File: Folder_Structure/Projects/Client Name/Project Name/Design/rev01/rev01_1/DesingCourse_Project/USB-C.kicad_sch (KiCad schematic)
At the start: 1 part, among them J7 TYPE-C-31-M-12

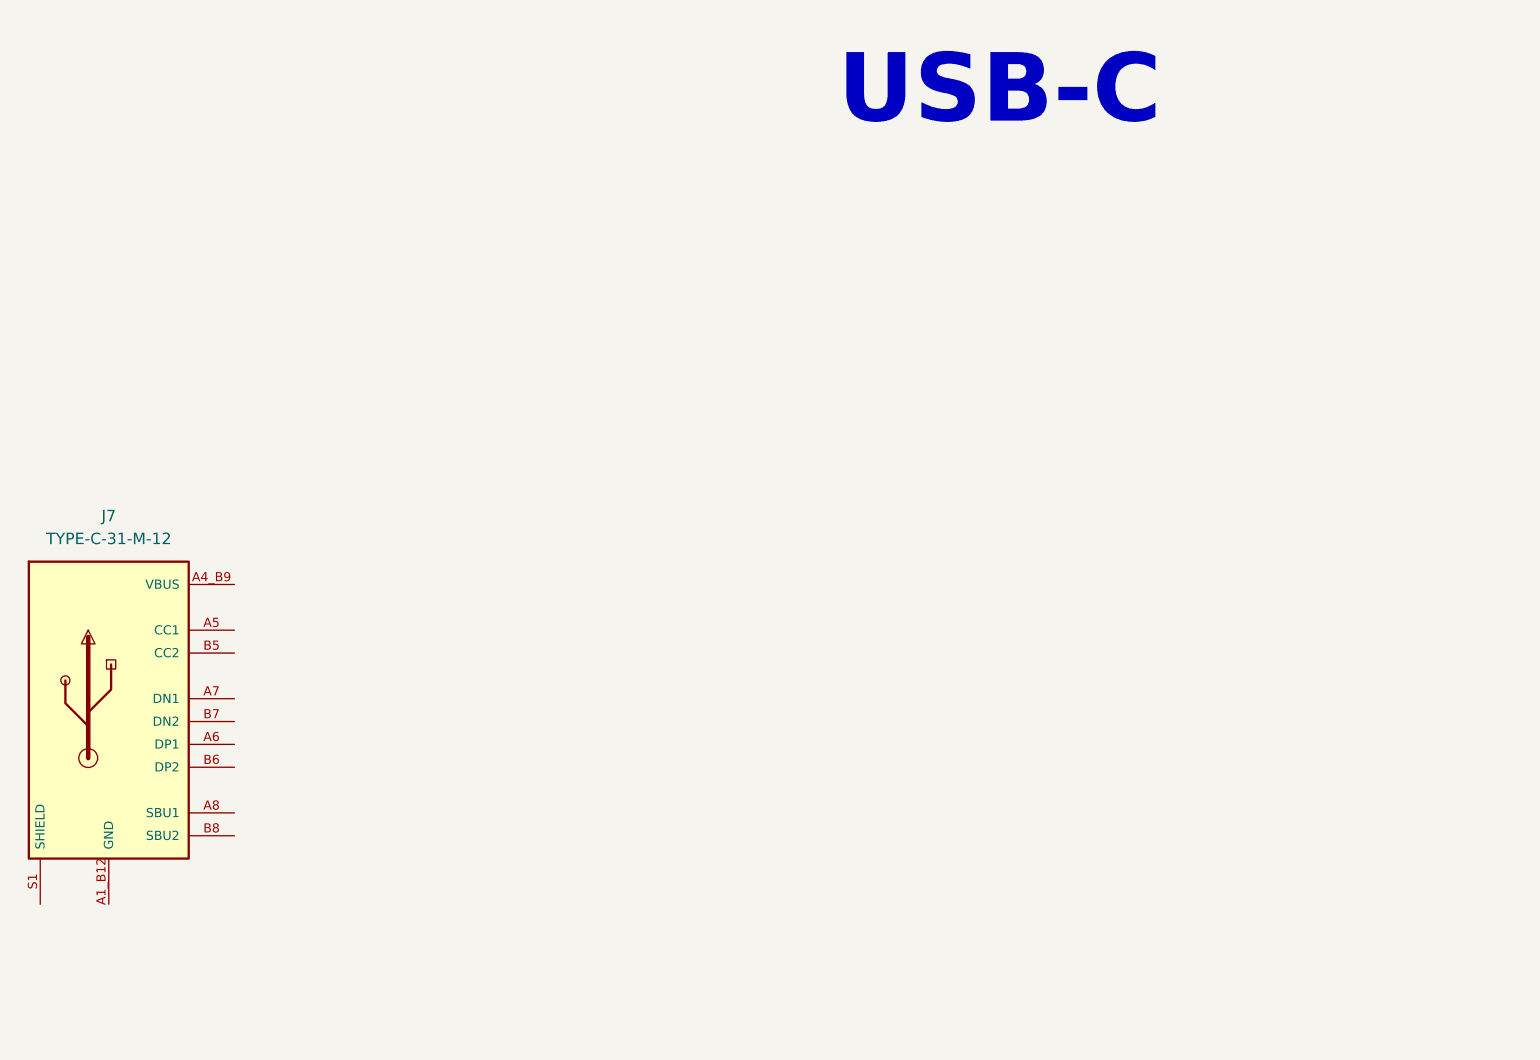
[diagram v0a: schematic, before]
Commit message: Update 9
USC-C & STEP_DOWN are DONE // MCU missing TVS diodes on P3V3 & P5V
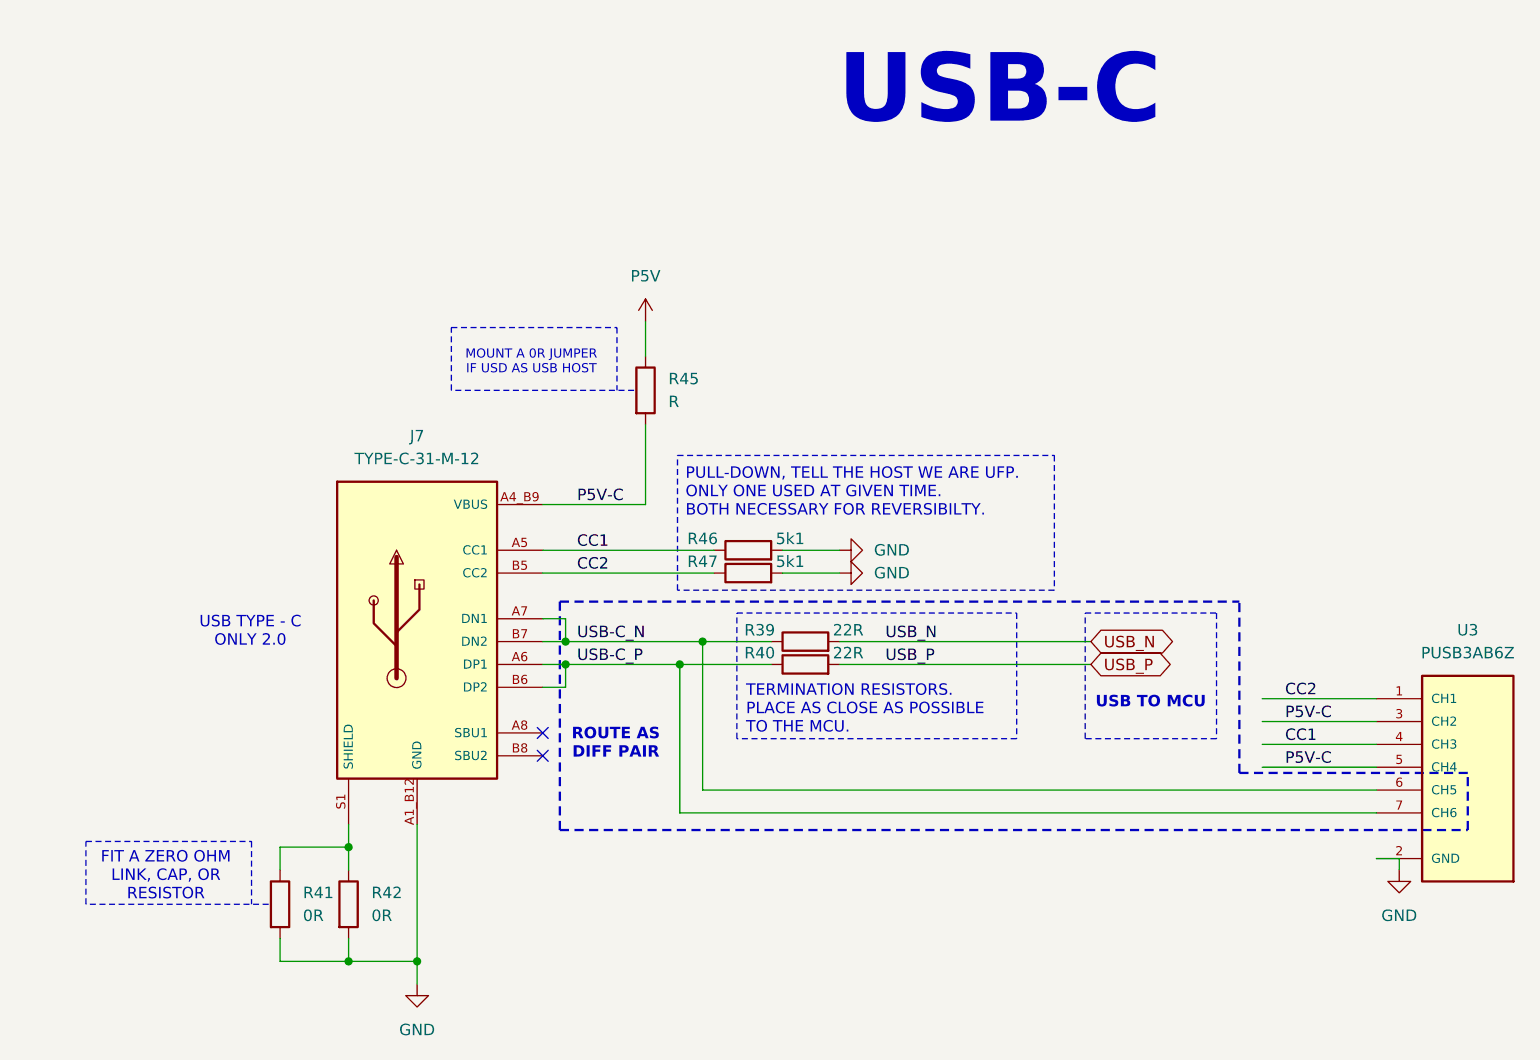
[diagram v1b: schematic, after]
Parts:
- added R39, R40: 22R, symbol Device:R
- added R41, R42: 0R, symbol Device:R
- added R45: R, symbol Device:R
- added R46, R47: 5k1, symbol Device:R
- added U3: PUSB3AB6Z, PUSB3AB6Z:IC_PUSB3AB6Z, symbol PUSB3AB6Z:PUSB3AB6Z
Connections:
- net GND: now also R41.2, R42.2, R46.2, R47.2, U3.2 (GND)
- net VBUS: now also R45.2, U3.3 (CH2), U3.5 (CH4)
- net CC1: now reaches J7.A5 (CC1)
- net CC1: now also R46.1, U3.4 (CH3)
- net USB-C_P: now reaches J7.A6 (DP1)
- net USB-C_P: now also J7.B6 (DP2), R40.1, U3.7 (CH6)
- net USB-C_N: now reaches J7.A7 (DN1)
- net USB-C_N: now also J7.B7 (DN2), R39.1, U3.6 (CH5)
- net CC2: now reaches J7.B5 (CC2)
- net CC2: now also R47.1, U3.1 (CH1)
- net at J7.S1 (SHIELD), J7.S2 (SHIELD), J7.S3 (SHIELD)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: now also R41.1, R42.1
- new net P5V: R45.1
- new net USB_N: R39.2
- new net USB_P: R40.2
- no-connect marks 0 -> 2
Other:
- note added: "FIT A ZERO OHM LINK, CAP, OR RESISTOR"
- note added: "MOUNT A 0R JUMPER IF USD AS USB HOST"
- note added: "PULL-DOWN, TELL THE HOST WE ARE UFP. ONLY ONE USED AT GIVEN TIME. BOTH NECESSARY FOR REVERSIBILTY."
- note added: "ROUTE AS DIFF PAIR"
- note added: "TERMINATION RESISTORS. PLACE AS CLOSE AS POSSIBLE TO THE MCU."
- note added: "USB TO MCU"
- note added: "USB TYPE - C ONLY 2.0"
- moved on the sheet: J7

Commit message: Update 12
Until STEP-DOWN page, all components have complete libraries.

Creation and incluison of all logos and labels libraries
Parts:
- removed R39, R40: 22R, symbol Device:R
- removed R41, R42: 0R, symbol Device:R
- removed R45: R, symbol Device:R
- removed R46, R47: 5k1, symbol Device:R
- added R2, R3, R4: 0R, Resistor_SMD:R_0603_1608Metric, symbol Device:R
- added R5, R6: 5k1, Resistor_SMD:R_0603_1608Metric, symbol Device:R
- added R7, R8: 22R, Resistor_SMD:R_0603_1608Metric, symbol Device:R
- U1: renamed from U3; Package XSON7-7 -> 7pin XSON7
- renumbered J7 to J2
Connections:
- net CC1: now also R5.1
- net CC2: now also R6.1
- net GND: now also R2.2, R3.2, R5.2, R6.2
- net P5V: now also R4.1
- net USB-C_N: now also R7.1
- net USB-C_P: now also R8.1
- net USB_N: now also R7.2
- net USB_P: now also R8.2
- net VBUS: now also R4.2
- net at J2.S1 (SHIELD), J2.S2 (SHIELD), J2.S3 (SHIELD)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: now also R2.1, R3.1

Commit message: Update 16
Initial component placement done
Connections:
- net VBUS: no longer U1.3 (CH2), U1.5 (CH4)
- new net P5V-C: U1.3 (CH2), U1.5 (CH4)

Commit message: Update17
Design rules and stack defined.

Check againg DR and proceed with layout.
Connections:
- net Shield_USB: now reaches J2.S1 (SHIELD), J2.S2 (SHIELD), J2.S3 (SHIELD), J2.S4 (SHIELD), R2.1, R3.1
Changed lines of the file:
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@@
+		)
+	)
+	(label "Shield_USB"
+		(at 87.63 104.14 180)
+		(effects
+			(font
+				(size 1.27 1.27)
+			)
+			(justify right bottom)
 		)
 	)

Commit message: Update18
Layout finished, clean up or layout and designators.
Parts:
- U1: Package 7pin XSON7 -> XSON7-7
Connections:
- net P5V-C is gone; now on net VBUS: U1.3 (CH2), U1.5 (CH4)
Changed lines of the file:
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@@
+		)
+	)
+	(label "P5V-C"
+		(at 113.03 66.04 0)
+		(effects
+			(font
+				(size 1.27 1.27)
+			)
+			(justify left bottom)
 		)
 	)
@@
 			)
 		)
-		(property "Description" "RES 0 OHM 0603 ±1% 1/10W"
+		(property "Description" "Resistor"
 			(at 80.01 110.49 0)
 			(effects
@@
 			)
 		)
-		(property "Description" "RES 5k1 OHM 0603 ±1% 1/10W"
+		(property "Description" "Resistor"
 			(at 132.08 71.12 0)
 			(effects
@@
 			)
 		)
-		(property "Description" "RES 5k1 OHM 0603 ±1% 1/10W"
+		(property "Description" "Resistor"
 			(at 132.08 73.66 0)
 			(effects
@@
 			)
 		)
-		(property "Description" "RES 22 OHM 0603 ±1% 1/10W"
+		(property "Description" "Resistor"
 			(at 138.43 81.28 0)
 			(effects
@@
 			)
 		)
-		(property "Description" "RES 0 OHM 0603 ±1% 1/10W"
+		(property "Description" "Resistor"
 			(at 120.65 53.34 0)
 			(effects
@@
 			)
 		)
-		(property "Package" "7pin XSON7"
+		(property "Package" "XSON7-7"
 			(at 212.09 97.79 0)
 			(effects
@@
 			)
 		)
-		(property "Description" "RES 0 OHM 0603 ±1% 1/10W"
+		(property "Description" "Resistor"
 			(at 87.63 110.49 0)
 			(effects
@@
 			)
 		)
-		(property "Description" "RES 22 OHM 0603 ±1% 1/10W"
+		(property "Description" "Resistor"
 			(at 138.43 83.82 0)
 			(effects
